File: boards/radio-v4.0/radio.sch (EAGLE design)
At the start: 29 parts, among them J1 HFW8R-1ST, J3 FTSH-105-01-F-D-K, U1 ISM43340, U2 MPM3620GQV-P

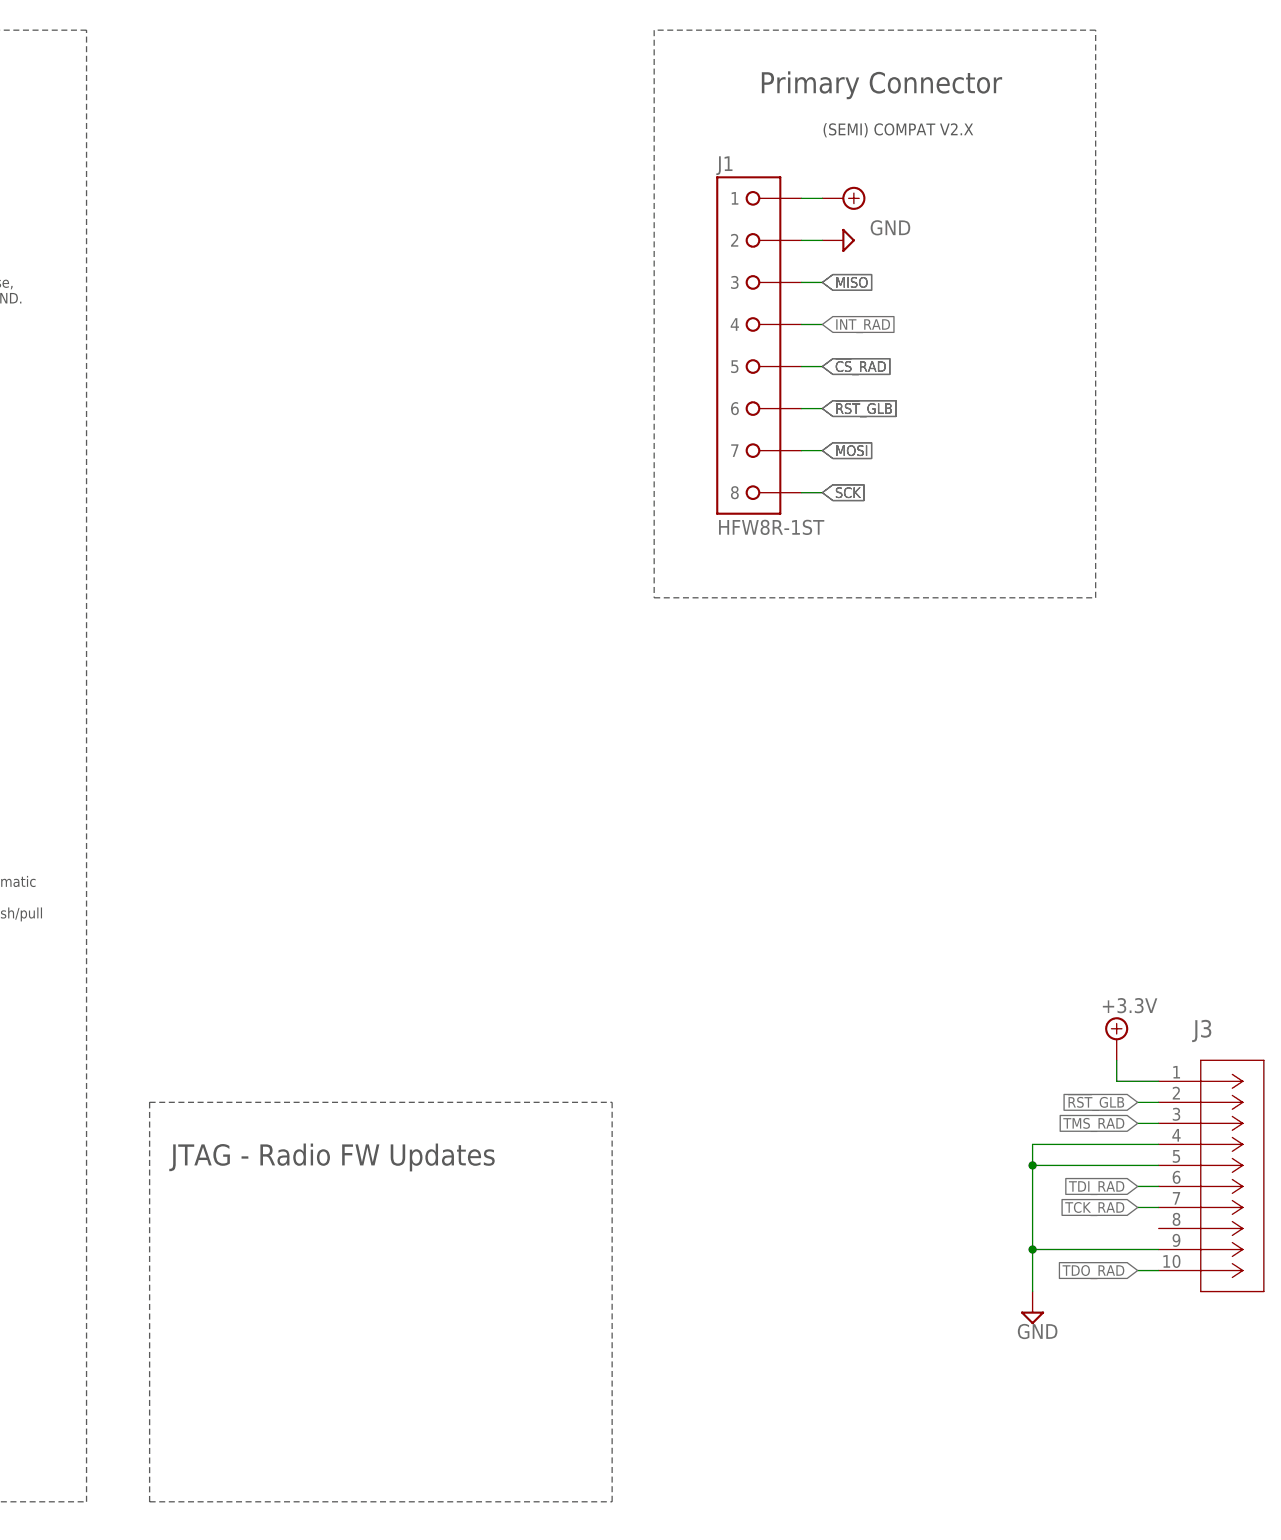
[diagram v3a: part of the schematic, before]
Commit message: Changed ffc connector for current one
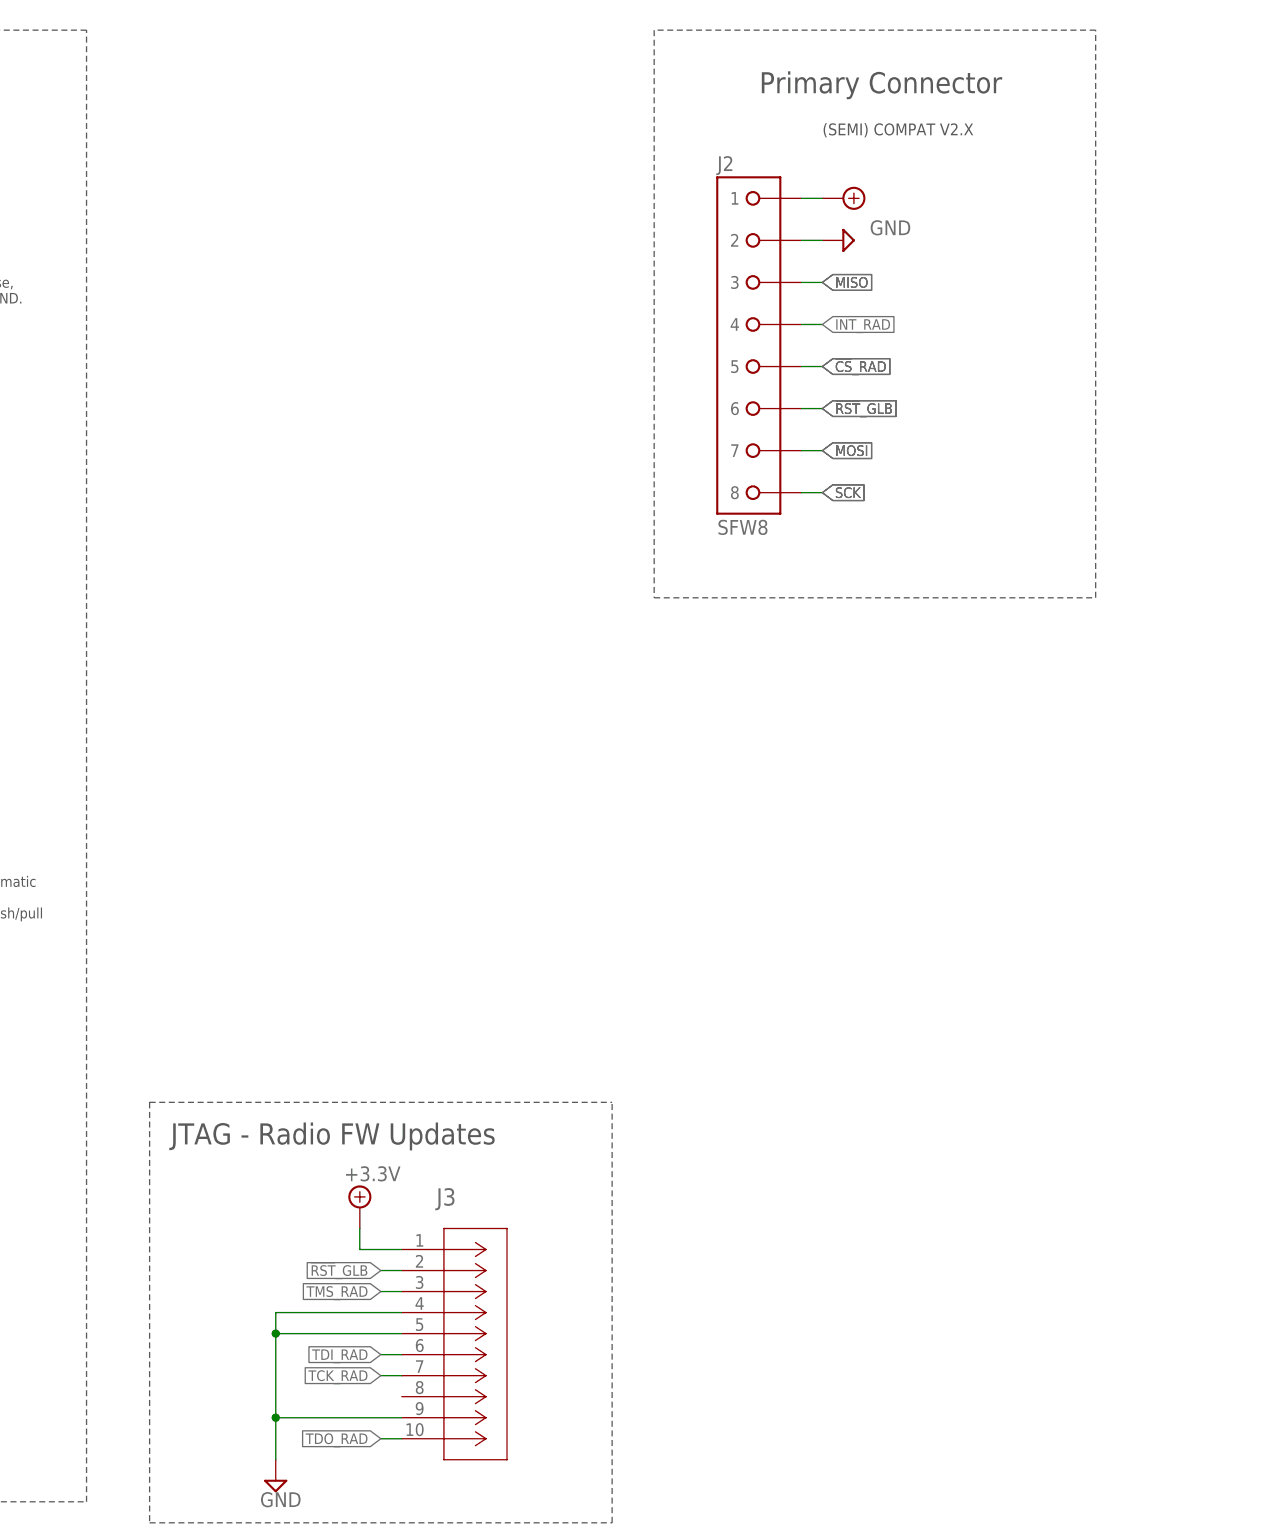
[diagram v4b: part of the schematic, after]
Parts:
- removed J1: HFW8R-1ST, RoboJackets-Connectors:HFW8R-1ST
- added J2: SFW8, RoboJackets-Connectors:SFW8
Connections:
- net !CS!_RAD: now also J2G$1.5; no longer J1G$1.5
- net !RST!_GLB: now also J2G$1.6; no longer J1G$1.6
- net +5.0V: now also J2G$1.1; no longer J1G$1.1
- net GND: now also J2G$1.2; no longer J1G$1.2
- net INT_RAD: now also J2G$1.4; no longer J1G$1.4
- net MISO: now also J2G$1.3; no longer J1G$1.3
- net MOSI: now also J2G$1.7; no longer J1G$1.7
- net SCK: now also J2G$1.8; no longer J1G$1.8
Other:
- moved on the sheet: J3
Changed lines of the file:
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@@
 <part name="SUPPLY9" library="RoboJackets-Supplies" deviceset="+5.0V" device=""/>
 <part name="SUPPLY10" library="supply2" library_urn="urn:adsk.eagle:library:372" deviceset="GND" device=""/>
-<part name="J1" library="RoboJackets-Connectors" deviceset="HFW8" device="R-1ST"/>
 <part name="C2" library="rcl" library_urn="urn:adsk.eagle:library:334" deviceset="C-US" device="C0805" package3d_urn="urn:adsk.eagle:package:23617/2" value="10uF"/>
 <part name="C3" library="rcl" library_urn="urn:adsk.eagle:library:334" deviceset="C-US" device="C0805" package3d_urn="urn:adsk.eagle:package:23617/2" value="10uF"/>
@@
 <part name="SUPPLY5" library="RoboJackets-Supplies" deviceset="+3.3V" device=""/>
 <part name="SUPPLY6" library="supply2" library_urn="urn:adsk.eagle:library:372" deviceset="GND" device=""/>
+<part name="J2" library="RoboJackets-Connectors" deviceset="SFW8" device=""/>
 </parts>
 <sheets>
@@
 <wire x1="248.92" y1="269.24" x2="248.92" y2="193.04" width="0.1524" layer="97" style="shortdash"/>
 <text x="190.5" y="264.16" size="2.54" layer="97">Debug LEDs</text>
-<wire x1="134.62" y1="55.88" x2="134.62" y2="7.62" width="0.1524" layer="97" style="shortdash"/>
-<wire x1="134.62" y1="7.62" x2="190.5" y2="7.62" width="0.1524" layer="97" style="shortdash"/>
+<wire x1="134.62" y1="55.88" x2="134.62" y2="5.08" width="0.1524" layer="97" style="shortdash"/>
+<wire x1="134.62" y1="5.08" x2="190.5" y2="5.08" width="0.1524" layer="97" style="shortdash"/>
 <wire x1="134.62" y1="55.88" x2="190.5" y2="55.88" width="0.1524" layer="97" style="shortdash"/>
-<text x="137.16" y="48.26" size="2.54" layer="97">JTAG - Radio FW Updates</text>
-<wire x1="190.5" y1="7.62" x2="190.5" y2="55.88" width="0.1524" layer="97" style="shortdash"/>
+<text x="137.16" y="50.8" size="2.54" layer="97">JTAG - Radio FW Updates</text>
+<wire x1="190.5" y1="5.08" x2="190.5" y2="55.88" width="0.1524" layer="97" style="shortdash"/>
 <text x="101.6" y="76.2" size="1.27" layer="97">Dev board ref schematic
 indicates IWIN LED
@@
 <attribute name="VALUE" x="221.615" y="160.655" size="1.778" layer="96"/>
 </instance>
-<instance part="J1" gate="G$1" x="208.28" y="147.32" smashed="yes">
-<attribute name="NAME" x="203.2" y="170.18" size="1.778" layer="95" font="vector" align="top-left"/>
-<attribute name="VALUE" x="203.2" y="124.46" size="1.778" layer="96" font="vector"/>
-</instance>
 <instance part="C2" gate="G$1" x="50.8" y="33.02" smashed="yes">
 <attribute name="NAME" x="51.816" y="33.655" size="1.778" layer="95"/>
@@
 <attribute name="NAME" x="42.1386" y="33.0708" size="1.778" layer="95" ratio="10" rot="SR0"/>
 </instance>
-<instance part="J3" gate="A" x="256.54" y="58.42" smashed="yes">
-<attribute name="NAME" x="260.7056" y="63.7286" size="2.0828" layer="95" ratio="6" rot="SR0"/>
-</instance>
-<instance part="SUPPLY5" gate="P" x="251.46" y="63.5" smashed="yes">
-<attribute name="VALUE" x="249.555" y="66.675" size="1.778" layer="96"/>
-</instance>
-<instance part="SUPPLY6" gate="GND" x="241.3" y="30.48" smashed="yes">
-<attribute name="VALUE" x="239.395" y="27.305" size="1.778" layer="96"/>
+<instance part="J3" gate="A" x="165.1" y="38.1" smashed="yes">
+<attribute name="NAME" x="169.2656" y="43.4086" size="2.0828" layer="95" ratio="6" rot="SR0"/>
+</instance>
+<instance part="SUPPLY5" gate="P" x="160.02" y="43.18" smashed="yes">
+<attribute name="VALUE" x="158.115" y="46.355" size="1.778" layer="96"/>
+</instance>
+<instance part="SUPPLY6" gate="GND" x="149.86" y="10.16" smashed="yes">
+<attribute name="VALUE" x="147.955" y="6.985" size="1.778" layer="96"/>
+</instance>
+<instance part="J2" gate="G$1" x="208.28" y="147.32" smashed="yes">
+<attribute name="NAME" x="203.2" y="170.18" size="1.778" layer="95" font="vector" align="top-left"/>
+<attribute name="VALUE" x="203.2" y="124.46" size="1.778" layer="96" font="vector"/>
 </instance>
 </instances>
@@
 <segment>
 <pinref part="J3" gate="A" pin="1"/>
-<wire x1="256.54" y1="58.42" x2="251.46" y2="58.42" width="0.1524" layer="91"/>
-<wire x1="251.46" y1="58.42" x2="251.46" y2="60.96" width="0.1524" layer="91"/>
+<wire x1="165.1" y1="38.1" x2="160.02" y2="38.1" width="0.1524" layer="91"/>
+<wire x1="160.02" y1="38.1" x2="160.02" y2="40.64" width="0.1524" layer="91"/>
 <pinref part="SUPPLY5" gate="P" pin="+3.3V"/>
 </segment>
@@
 </segment>
 <segment>
-<pinref part="J1" gate="G$1" pin="2"/>
 <wire x1="213.36" y1="160.02" x2="215.9" y2="160.02" width="0.1524" layer="91"/>
 <pinref part="SUPPLY10" gate="GND" pin="GND"/>
+<pinref part="J2" gate="G$1" pin="2"/>
 </segment>
 <segment>
 <pinref part="J3" gate="A" pin="5"/>
-<wire x1="256.54" y1="48.26" x2="241.3" y2="48.26" width="0.1524" layer="91"/>
-<wire x1="241.3" y1="48.26" x2="241.3" y2="38.1" width="0.1524" layer="91"/>
+<wire x1="165.1" y1="27.94" x2="149.86" y2="27.94" width="0.1524" layer="91"/>
+<wire x1="149.86" y1="27.94" x2="149.86" y2="17.78" width="0.1524" layer="91"/>
 <pinref part="J3" gate="A" pin="4"/>
-<wire x1="241.3" y1="38.1" x2="241.3" y2="33.02" width="0.1524" layer="91"/>
-<wire x1="256.54" y1="50.8" x2="241.3" y2="50.8" width="0.1524" layer="91"/>
-<wire x1="241.3" y1="50.8" x2="241.3" y2="48.26" width="0.1524" layer="91"/>
-<junction x="241.3" y="48.26"/>
+<wire x1="149.86" y1="17.78" x2="149.86" y2="12.7" width="0.1524" layer="91"/>
+<wire x1="165.1" y1="30.48" x2="149.86" y2="30.48" width="0.1524" layer="91"/>
+<wire x1="149.86" y1="30.48" x2="149.86" y2="27.94" width="0.1524" layer="91"/>
+<junction x="149.86" y="27.94"/>
 <pinref part="J3" gate="A" pin="9"/>
-<wire x1="256.54" y1="38.1" x2="241.3" y2="38.1" width="0.1524" layer="91"/>
-<junction x="241.3" y="38.1"/>
+<wire x1="165.1" y1="17.78" x2="149.86" y2="17.78" width="0.1524" layer="91"/>
+<junction x="149.86" y="17.78"/>
 <pinref part="SUPPLY6" gate="GND" pin="GND"/>
 </segment>
@@
 <segment>
 <pinref part="J3" gate="A" pin="3"/>
-<wire x1="256.54" y1="53.34" x2="254" y2="53.34" width="0.1524" layer="91"/>
-<label x="254" y="53.34" size="1.27" layer="95" rot="R180" xref="yes"/>
+<wire x1="165.1" y1="33.02" x2="162.56" y2="33.02" width="0.1524" layer="91"/>
+<label x="162.56" y="33.02" size="1.27" layer="95" rot="R180" xref="yes"/>
 </segment>
 </net>
@@
 <segment>
 <pinref part="J3" gate="A" pin="7"/>
-<wire x1="256.54" y1="43.18" x2="254" y2="43.18" width="0.1524" layer="91"/>
-<label x="254" y="43.18" size="1.27" layer="95" rot="R180" xref="yes"/>
+<wire x1="165.1" y1="22.86" x2="162.56" y2="22.86" width="0.1524" layer="91"/>
+<label x="162.56" y="22.86" size="1.27" layer="95" rot="R180" xref="yes"/>
 </segment>
 </net>
@@
 <segment>
 <pinref part="J3" gate="A" pin="6"/>
-<wire x1="256.54" y1="45.72" x2="254" y2="45.72" width="0.1524" layer="91"/>
-<label x="254" y="45.72" size="1.27" layer="95" rot="R180" xref="yes"/>
+<wire x1="165.1" y1="25.4" x2="162.56" y2="25.4" width="0.1524" layer="91"/>
+<label x="162.56" y="25.4" size="1.27" layer="95" rot="R180" xref="yes"/>
 </segment>
 </net>
@@
 <segment>
 <pinref part="J3" gate="A" pin="10"/>
-<wire x1="256.54" y1="35.56" x2="254" y2="35.56" width="0.1524" layer="91"/>
-<label x="254" y="35.56" size="1.27" layer="95" rot="R180" xref="yes"/>
+<wire x1="165.1" y1="15.24" x2="162.56" y2="15.24" width="0.1524" layer="91"/>
+<label x="162.56" y="15.24" size="1.27" layer="95" rot="R180" xref="yes"/>
 </segment>
 </net>
@@
 </segment>
 <segment>
-<pinref part="J1" gate="G$1" pin="1"/>
 <wire x1="213.36" y1="165.1" x2="215.9" y2="165.1" width="0.1524" layer="91"/>
 <pinref part="SUPPLY9" gate="P" pin="+5.0V"/>
+<pinref part="J2" gate="G$1" pin="1"/>
 </segment>
 </net>
@@
 <wire x1="213.36" y1="139.7" x2="215.9" y2="139.7" width="0.1524" layer="91"/>
 <label x="215.9" y="139.7" size="1.27" layer="95" xref="yes"/>
-<pinref part="J1" gate="G$1" pin="6"/>
+<pinref part="J2" gate="G$1" pin="6"/>
 </segment>
 <segment>
@@
 <segment>
 <pinref part="J3" gate="A" pin="2"/>
-<wire x1="256.54" y1="55.88" x2="254" y2="55.88" width="0.1524" layer="91"/>
-<label x="254" y="55.88" size="1.27" layer="95" rot="R180" xref="yes"/>
+<wire x1="165.1" y1="35.56" x2="162.56" y2="35.56" width="0.1524" layer="91"/>
+<label x="162.56" y="35.56" size="1.27" layer="95" rot="R180" xref="yes"/>
 </segment>
 </net>
@@
 <segment>
 <label x="215.9" y="134.62" size="1.27" layer="95" xref="yes"/>
-<pinref part="J1" gate="G$1" pin="7"/>
 <wire x1="213.36" y1="134.62" x2="215.9" y2="134.62" width="0.1524" layer="91"/>
 <label x="215.9" y="134.62" size="1.27" layer="95" xref="yes"/>
+<pinref part="J2" gate="G$1" pin="7"/>
 </segment>
 </net>
@@
 <segment>
 <label x="215.9" y="129.54" size="1.27" layer="95" xref="yes"/>
-<pinref part="J1" gate="G$1" pin="8"/>
 <wire x1="213.36" y1="129.54" x2="215.9" y2="129.54" width="0.1524" layer="91"/>
 <label x="215.9" y="129.54" size="1.27" layer="95" xref="yes"/>
+<pinref part="J2" gate="G$1" pin="8"/>
 </segment>
 </net>
@@
 <wire x1="213.36" y1="144.78" x2="215.9" y2="144.78" width="0.1524" layer="91"/>
 <label x="215.9" y="144.78" size="1.27" layer="95" xref="yes"/>
-<pinref part="J1" gate="G$1" pin="5"/>
+<pinref part="J2" gate="G$1" pin="5"/>
 </segment>
 <segment>
@@
 <wire x1="213.36" y1="149.86" x2="215.9" y2="149.86" width="0.1524" layer="91"/>
 <label x="215.9" y="149.86" size="1.27" layer="95" xref="yes"/>
-<pinref part="J1" gate="G$1" pin="4"/>
+<pinref part="J2" gate="G$1" pin="4"/>
 </segment>
 <segment>
@@
 <wire x1="213.36" y1="154.94" x2="215.9" y2="154.94" width="0.1524" layer="91"/>
 <label x="215.9" y="154.94" size="1.27" layer="95" xref="yes"/>
-<pinref part="J1" gate="G$1" pin="3"/>
-</segment>
-<segment>
+<pinref part="J2" gate="G$1" pin="3"/>
+</segment>
+<segment>

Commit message: Moved plane
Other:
- note removed: "(SEMI) COMPAT V2.X"
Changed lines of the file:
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@@
 are in a passthrough
 enabled state.</text>
-<text x="215.9" y="172.72" size="1.4224" layer="97">(SEMI) COMPAT V2.X</text>
 <text x="96.52" y="152.4" size="1.27" layer="97">Pin left floating on purpose,
 internally connected to GND.</text>
